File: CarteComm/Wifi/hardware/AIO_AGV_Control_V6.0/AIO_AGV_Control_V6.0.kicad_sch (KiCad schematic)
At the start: 59 parts, among them J1 DB25_Pins, J2 DB25_Socket, J3 Conn_Coaxial_Small, T1 IRF520, T10 IRF520, T11 IRF520, T12 IRF520, T14 IRF520, T15 IRF520, T16 IRF520, T17 IRF520, T18 IRF520, T19 IRF520, T2 IRF520, T20 IRF520, T21 IRF520, T22 IRF520, T23 IRF520, T24 IRF520, T3 IRF520, T4 IRF520, T5 IRF520, T6 IRF520, T7 IRF520, T8 IRF520, T9 IRF520, U1 ESP32-DEVKITC, U2 RFM95W-868S2

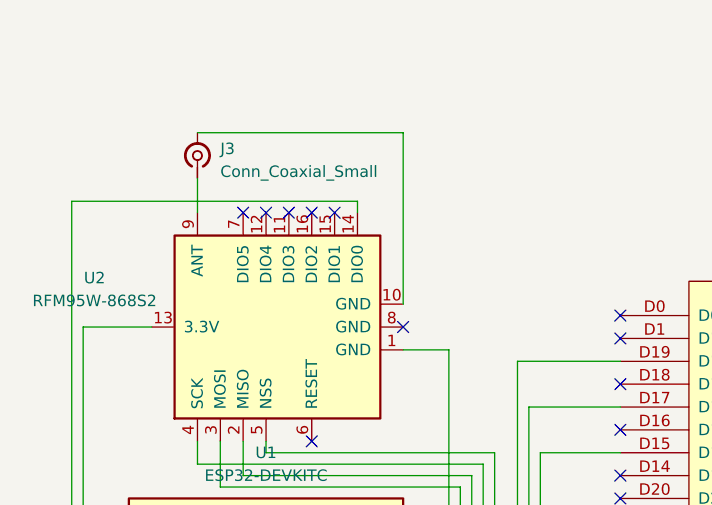
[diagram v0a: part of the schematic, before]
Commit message: feat(lora): remplacer la passerelle MQTT par une passerelle LoRa dans A2 et A3
Vous aviez raison de relever l'incohérence : ces deux architectures n'ont ni
broker, ni réseau d'entreprise, et leur firmware ESP32 portait pourtant un
GatewayApp qui publiait sur des topics et dépendait d'IMqttPublisher. Je l'avais
laissé en dette plutôt que de l'écrire.

LoraGatewayApp le remplace. Il rend exactement le même service côté ATmega -
mêmes trames de liaison, même heartbeat, même repli de sécurité - et change
seulement la source des ordres : trames applicatives de 9 octets sur ITransport,
accusé renvoyé par la même voie, idempotence (node_id, seq) en table locale.

Le budget de rapport cyclique s'applique aussi aux accusés, parce qu'un
récepteur qui acquitte est un émetteur. Un accusé refusé faute de budget est
compté, pas perdu en silence.

Le firmware ESP32 est réécrit : plus de Wi-Fi STA ni de client MQTT, mais SPI +
Sx1276Radio + LoraTransport, avec le brochage relevé sur votre V6.0 dans
board_pins.h - IO5, IO18, IO19, IO23, IO26, et kLoraReset à 0xFF puisque la
broche RESET du RFM95W n'est pas connectée au PCB.

MqttConfig et WifiConfig quittent le profil, la section lora: y entre, et
aes_enabled passe à true : sans TLS, le chiffrement applicatif est la seule
protection de la liaison radio. Le champ mqtt_up de /agvdump est conservé
volontairement - c'est un contrat d'atelier, il porte désormais l'état radio.

Deux défauts trouvés en écrivant les tests, et corrigés. La détection de silence
de l'ATmega utilisait 0 comme sentinelle « jamais reçu », alors que c'est un
instant valide au démarrage. Et surtout, les quatre Makefile ne suivaient pas
les dépendances d'en-têtes : modifier une classe ne recompilait pas ses
utilisateurs, on reliait des objets compilés contre deux versions de la même
classe, et un test échouait sans qu'aucune erreur ne soit signalée. -MMD -MP
partout.

Kanban LG1 soldé. 470 tests verts, dont 10 nouveaux sur la passerelle.

Co-Authored-By: Claude Opus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
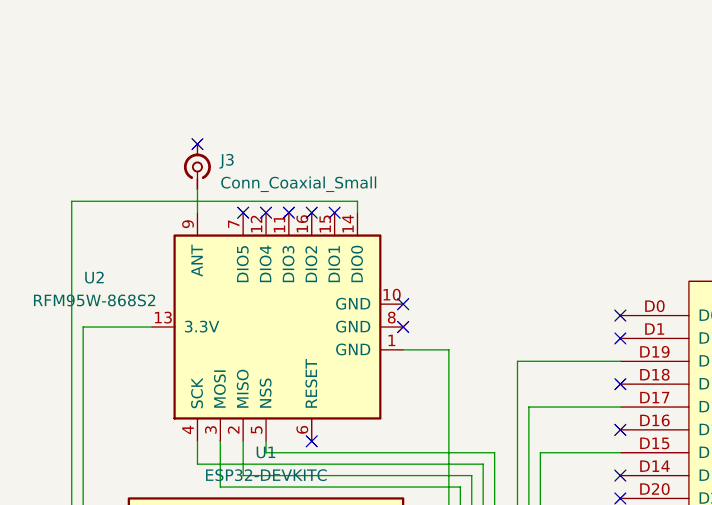
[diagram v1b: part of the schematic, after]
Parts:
- J3: footprint Connector_Coaxial:SMA_Amphenol_901-143_Horizontal -> Connector_Coaxial:SMA_BAT_Wireless_BWSMA-KWE-Z001
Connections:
- net at U2.10 (GND): no longer J3.2 (Ext)
- no-connect marks 71 -> 73
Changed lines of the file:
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@@
 	)
 	(no_connect
+		(at 26.67 24.13)
+	)
+	(no_connect
+		(at 49.53 41.91)
+	)
+	(no_connect
 		(at 73.66 109.22)
 	)
@@
 	(wire
 		(pts
-			(xy 26.67 22.86) (xy 49.53 22.86)
-		)
-		(stroke
-			(width 0)
-			(type default)
-		)
-	)
-	(wire
-		(pts
 			(xy 255.27 129.54) (xy 255.27 139.7)
 		)
@@
 	(wire
 		(pts
+			(xy 26.67 29.21) (xy 26.67 31.75)
+		)
+		(stroke
+			(width 0)
+			(type default)
+		)
+	)
+	(wire
+		(pts
 			(xy 274.32 109.22) (xy 280.67 109.22)
 		)
@@
 	(wire
 		(pts
-			(xy 26.67 27.94) (xy 26.67 31.75)
-		)
-		(stroke
-			(width 0)
-			(type default)
-		)
-	)
-	(wire
-		(pts
 			(xy 58.42 86.36) (xy 58.42 59.69)
 		)
@@
 	(wire
 		(pts
-			(xy 49.53 22.86) (xy 49.53 41.91)
-		)
-		(stroke
-			(width 0)
-			(type default)
-		)
-	)
-	(wire
-		(pts
 			(xy 143.51 168.91) (xy 143.51 184.15)
 		)
@@
 	)
 	(symbol
-		(lib_id "Connector:Conn_Coaxial_Small")
-		(at 26.67 25.4 90)
-		(unit 1)
-		(body_style 1)
-		(exclude_from_sim no)
-		(in_bom yes)
-		(on_board yes)
-		(in_pos_files yes)
-		(dnp no)
-		(fields_autoplaced yes)
-		(property "Reference" "J3"
-			(at 29.21 24.6494 90)
-			(show_name no)
-			(do_not_autoplace no)
-			(effects
-				(font
-					(size 1.27 1.27)
-				)
-				(justify right)
-			)
-		)
-		(property "Value" "Conn_Coaxial_Small"
-			(at 29.21 27.1894 90)
-			(show_name no)
-			(do_not_autoplace no)
-			(effects
-				(font
-					(size 1.27 1.27)
-				)
-				(justify right)
-			)
-		)
-		(property "Footprint" "Connector_Coaxial:SMA_Amphenol_901-143_Horizontal"
-			(at 26.67 25.4 0)
-			(hide yes)
-			(show_name no)
-			(do_not_autoplace no)
-			(effects
-				(font
-					(size 1.27 1.27)
-				)
-			)
-		)
-		(property "Datasheet" ""
-			(at 26.67 25.4 0)
-			(hide yes)
-			(show_name no)
-			(do_not_autoplace no)
-			(effects
-				(font
-					(size 1.27 1.27)
-				)
-			)
-		)
-		(property "Description" "small coaxial connector (BNC, SMA, SMB, SMC, Cinch/RCA, LEMO, ...)"
-			(at 26.67 25.4 0)
-			(hide yes)
-			(show_name no)
-			(do_not_autoplace no)
-			(effects
-				(font
-					(size 1.27 1.27)
-				)
-			)
-		)
-		(pin "2"
-		)
-		(pin "1"
-		)
-		(instances
-			(project "AIO_AGV_Control_V6.0"
-				(path "/8c8bc9e4-6813-466f-a699-de8b6f087fa1"
-					(reference "J3")
-					(unit 1)
-				)
-			)
-		)
-	)
-	(symbol
 		(lib_id "IRF520:IRF520")
 		(at 238.76 130.81 0)
@@
 					(unit 1)
 				)
+			)
+		)
+	)
+	(symbol
+		(lib_id "Connector:Conn_Coaxial_Small")
+		(at 26.67 26.67 90)
+		(unit 1)
+		(body_style 1)
+		(exclude_from_sim no)
+		(in_bom yes)
+		(on_board yes)
+		(in_pos_files yes)
+		(dnp no)
+		(fields_autoplaced yes)
+		(property "Reference" "J3"
+			(at 29.21 25.9194 90)
+			(show_name no)
+			(do_not_autoplace no)
+			(effects
+				(font
+					(size 1.27 1.27)
+				)
+				(justify right)
+			)
+		)
+		(property "Value" "Conn_Coaxial_Small"
+			(at 29.21 28.4594 90)
+			(show_name no)
+			(do_not_autoplace no)
+			(effects
+				(font
+					(size 1.27 1.27)
+				)
+				(justify right)
+			)
+		)
+		(property "Footprint" "Connector_Coaxial:SMA_BAT_Wireless_BWSMA-KWE-Z001"
+			(at 26.67 26.67 0)
+			(hide yes)
+			(show_name no)
+			(do_not_autoplace no)
+			(effects
+				(font
+					(size 1.27 1.27)
+				)
+			)
+		)
+		(property "Datasheet" ""
+			(at 26.67 26.67 0)
+			(hide yes)
+			(show_name no)
+			(do_not_autoplace no)
+			(effects
+				(font
+					(size 1.27 1.27)
+				)
+			)
+		)
+		(property "Description" "small coaxial connector (BNC, SMA, SMB, SMC, Cinch/RCA, LEMO, ...)"
+			(at 26.67 26.67 0)
+			(hide yes)
+			(show_name no)
+			(do_not_autoplace no)
+			(effects
+				(font
+					(size 1.27 1.27)
+				)
+			)
+		)
+		(pin "1"
+		)
+		(pin "2"
+		)
+		(instances
+			(project "AIO_AGV_Control_V6.0"
+				(path "/8c8bc9e4-6813-466f-a699-de8b6f087fa1"
+					(reference "J3")
+					(unit 1)
+				)
